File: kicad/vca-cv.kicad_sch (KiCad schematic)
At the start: 11 parts, among them Q7 2N3906, U9 TL072

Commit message: Minor tweaks and additional comments
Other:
- note added: "TODO calculate these values"
- note added: "i_vca ma = Vc/Rin * (1k + 33k)/1k 5V input so 5v/330 * 34 = 0.51ma"
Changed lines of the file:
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@@
     (stroke (width 0) (type default))
+  )
+  (text "i_vca ma = Vc/Rin * (1k + 33k)/1k\n\n5V input so 5v/330 * 34 = 0.51ma"
+    (at 176.53 107.95 0)
+    (effects (font (size 1.27 1.27)) (justify left bottom))
+  )
+  (text "TODO calculate these values" (at 153.67 50.8 0)
+    (effects (font (size 1.27 1.27)) (justify left bottom))
   )
   (hierarchical_label "VCA_LEVEL" (shape input) (at 96.52 95.25 180) (fields_autoplaced)

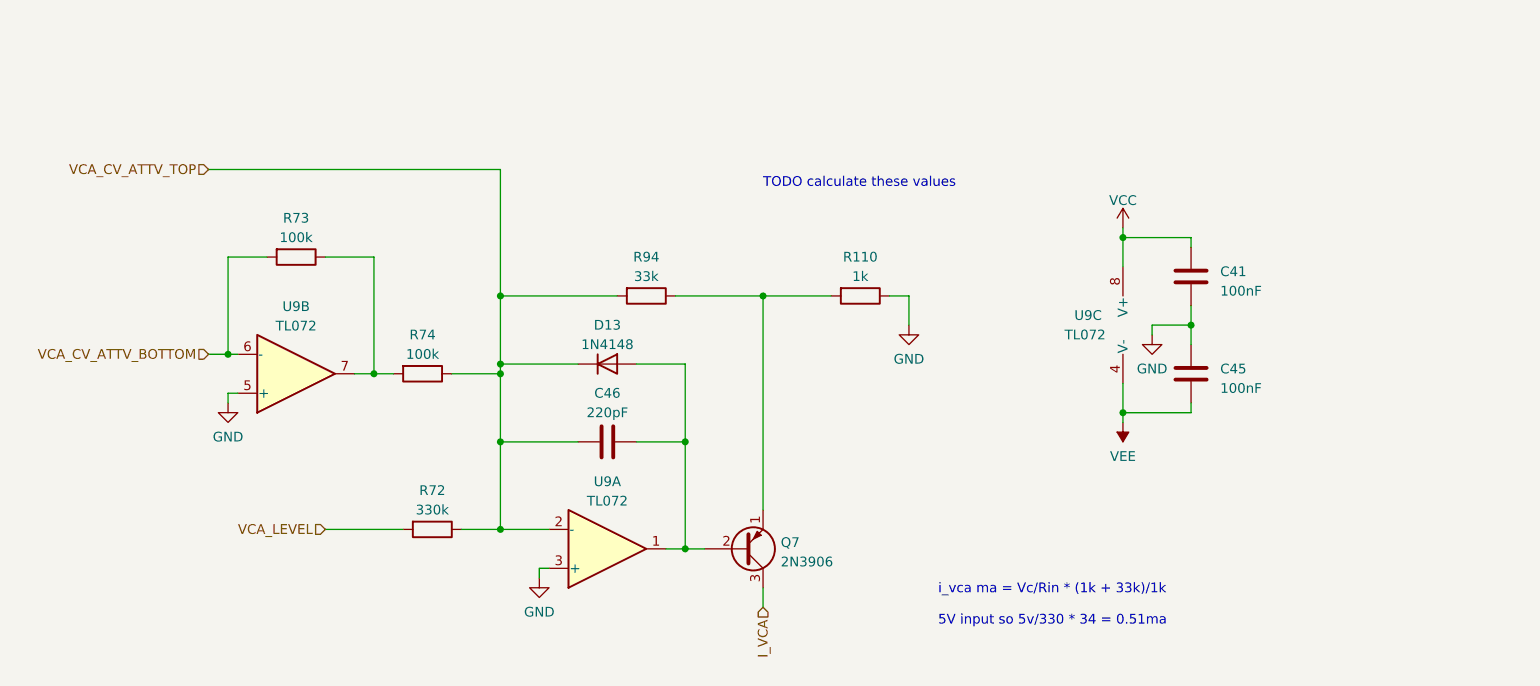
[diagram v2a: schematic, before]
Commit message: Updating board for new footprint libraries
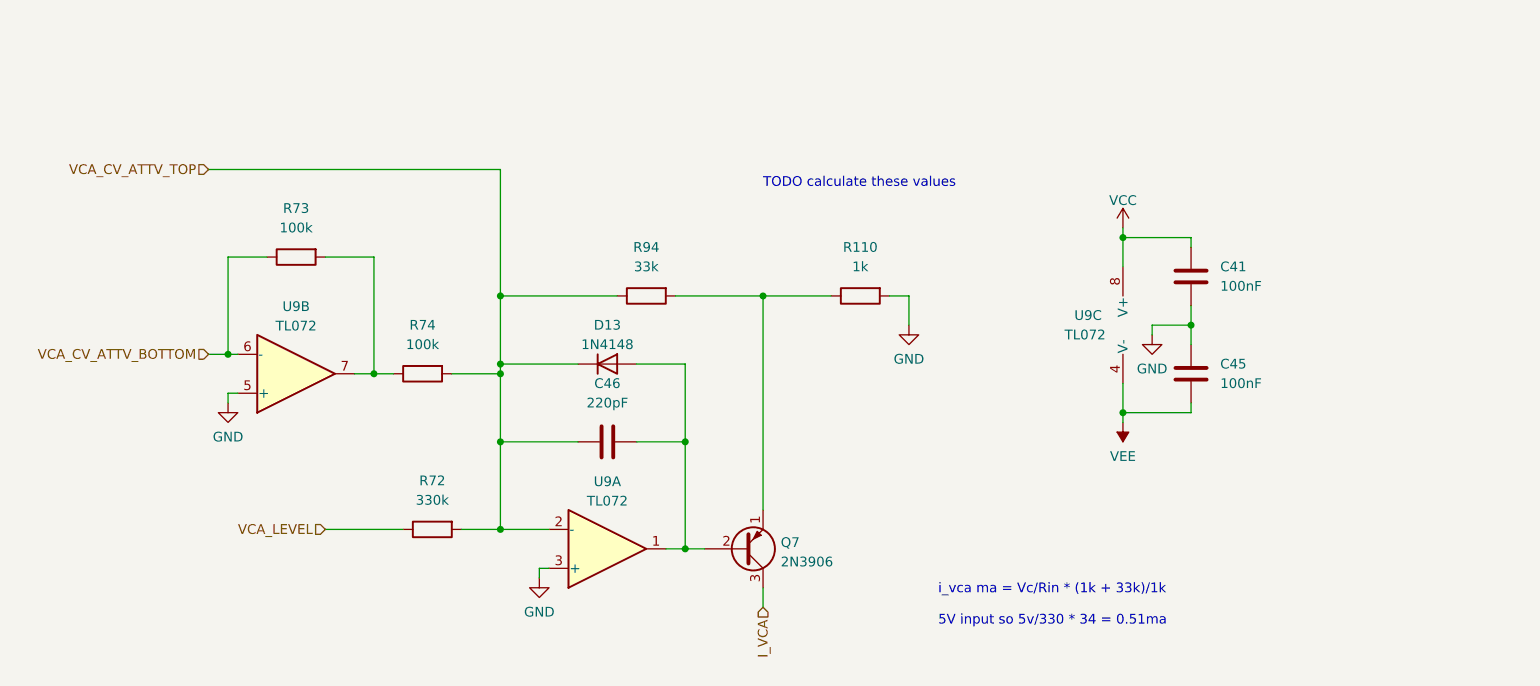
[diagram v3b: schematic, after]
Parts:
- C41, C45, C46: symbol Rumblesan Standard Parts:C -> Rumblesan_Standard_Parts:C
- Q7: footprint Rumblesan_Standard_Parts:TO-92_Inline_Wide -> Package_TO_SOT_THT:TO-92_Inline_Wide
- R110, R72, R73, R74, R94: symbol Rumblesan Standard Parts:R -> Rumblesan_Standard_Parts:R
- U9: footprint Rumblesan_Standard_Parts:DIP-8_W7.62mm_Socket -> Package_DIP:DIP-8_W7.62mm_Socket
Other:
- moved on the sheet: R110, R72, R73, R74, R94

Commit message: Updating with rev03 changes
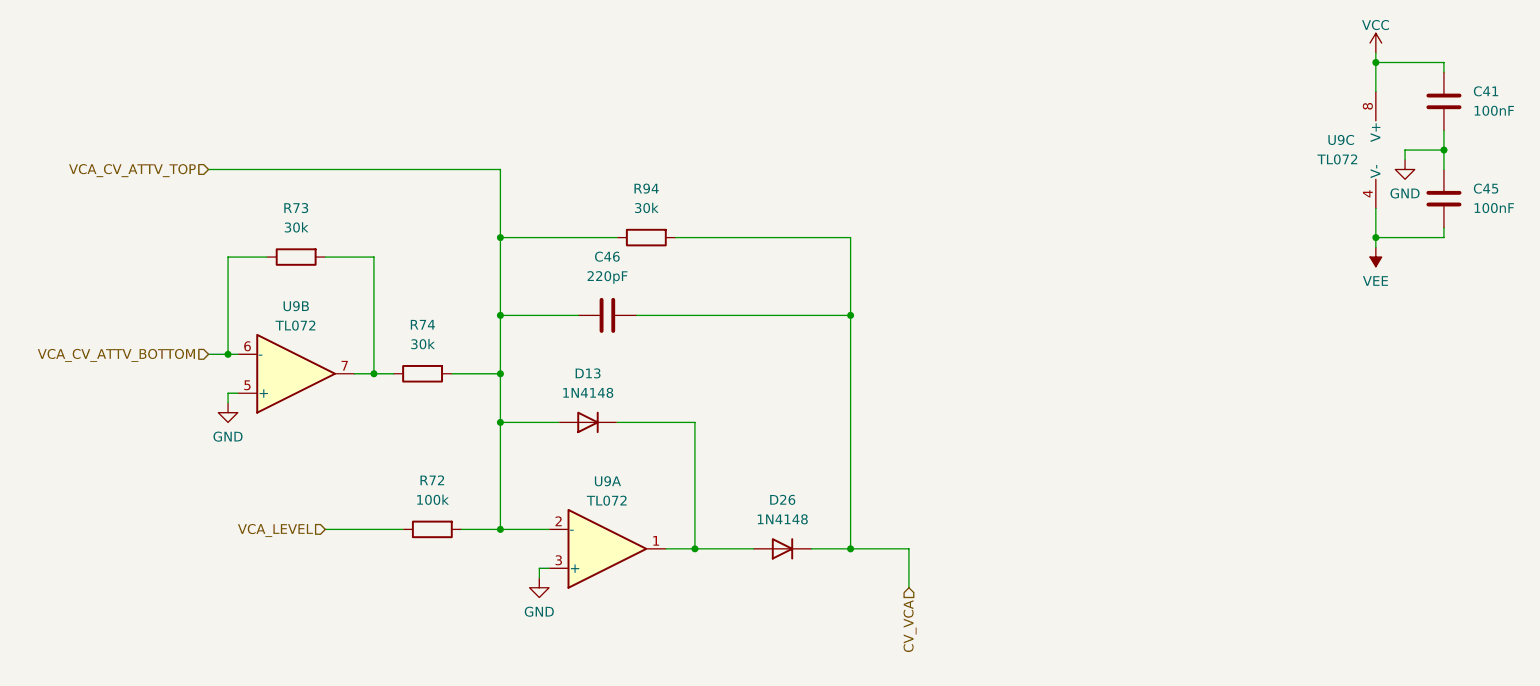
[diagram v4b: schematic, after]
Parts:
- removed Q7: 2N3906, Package_TO_SOT_THT:TO-92_Inline_Wide, symbol Transistor_BJT:2N3906
- removed R110: 1k, Rumblesan_Standard_Parts:R_Axial_DIN0207_L6.3mm_D2.5mm_P10.16mm_Horizontal, symbol Rumblesan_Standard_Parts:R
- added D26: 1N4148, Rumblesan_Standard_Parts:D_DO-35_SOD27_P7.62mm_Horizontal, symbol Device:D
- R72: value 330k -> 100k
- R73, R74: value 100k -> 30k
- R94: value 33k -> 30k
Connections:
- net VCA_CV_ATTV_TOP: now also D13.2 (A); no longer D13.1 (K)
- net CV_VCA: now reaches R94.1
- net CV_VCA: now also C46.2, D26.1 (K)
- new net: D13.1 (K), D26.2 (A), U9.1
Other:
- note removed: "TODO calculate these values"
- note removed: "i_vca ma = Vc/Rin * (1k + 33k)/1k 5V input so 5v/330 * 34 = 0.51ma"
- moved on the sheet: C41, C45, C46, D13, R94, U9C
